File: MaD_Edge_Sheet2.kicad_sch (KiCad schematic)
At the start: 105 parts

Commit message: new Mad Edge being manufactured
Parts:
- removed C? (x6): 0.1uF, symbol Device:C_Small
- removed D? (x6): LED, symbol Device:LED
- removed IC, IC? (x3): NSI50010YT1G, symbol NSI50010YT1G:NSI50010YT1G
- removed IC?: ISO6742DWR, symbol ISO6742DWR:ISO6742DWR
- removed IC?: ISO6721BDR, symbol ISO6721BDR:ISO6721BDR
- removed J?: DYNPWR, symbol Connector_Generic:Conn_01x03
- removed J?: ServoCtrl, symbol Connector_Generic:Conn_01x10
- removed J?: Encoder, symbol Connector_Generic:Conn_01x10
- removed J?: ServoSerial, symbol Connector_Generic:Conn_01x05
- removed JP?: Z_GND, symbol Jumper:Jumper_2_Open
- removed JP?: ZI_GND, symbol Jumper:Jumper_2_Open
- removed JP?: A_GND, symbol Jumper:Jumper_2_Open
- removed JP?: TTL-SINK, symbol Jumper:Jumper_3_Open
- removed JP?: B_GND, symbol Jumper:Jumper_2_Open
- removed Q?: 2N3904, Package_TO_SOT_THT:TO-92_Inline, symbol Transistor_BJT:2N3904
- removed R? (x5): 1K, symbol Device:R_Small
- removed R? (x6): 220R, symbol Device:R_Small
- removed R?: 43K, symbol Device:R_Small
- removed U? (x2): VO2631, Package_DIP:DIP-8_W7.62mm, symbol Isolator:VO2631
- removed U?: AM26LS31CD, Package_SO:SOIC-16_3.9x9.9mm_P1.27mm, symbol Interface:AM26LS31CD
- added C13, C18, C19, C23, C7, C9: 0.1uF, Capacitor_SMD:C_0603_1608Metric, symbol Device:C_Small
- added C17, C5: 10uF, Capacitor_SMD:C_1206_3216Metric, symbol Device:C_Small
- added D10, D11, D13, D16, D5, D7, D8: LED, LED_SMD:LED_0603_1608Metric, symbol Device:LED
- added IC1: ISO6742DWR, ISO6742DWR:SOIC127P1030X265-16N, symbol ISO6742DWR:ISO6742DWR
- added IC12, IC13: NSI50010YT1G, NSI50010YT1G:SOD3716X135N, symbol NSI50010YT1G:NSI50010YT1G
- added IC3: UCC12040DVER, UCC12040DVER:SOIC127P1030X265-16N, symbol UCC12040DVER:UCC12040DVER
- added J10: ChargePump, Connector_Molex:Molex_Micro-Fit_3.0_43650-0321_1x03_P3.00mm_Vertical, symbol Connector_Generic:Conn_01x03
- added J17: GPI_3, Connector_Molex:Molex_Micro-Fit_3.0_43650-0321_1x03_P3.00mm_Vertical, symbol Connector_Generic:Conn_01x03
- added J18: GPI_4, Connector_Molex:Molex_Micro-Fit_3.0_43650-0321_1x03_P3.00mm_Vertical, symbol Connector_Generic:Conn_01x03
- added J5: GPO_2, Connector_Molex:Molex_Micro-Fit_3.0_43045-0415_2x02_P3.00mm_Vertical, symbol Connector_Generic:Conn_01x04
- added J6: GPO_1, Connector_Molex:Molex_Micro-Fit_3.0_43045-0415_2x02_P3.00mm_Vertical, symbol Connector_Generic:Conn_01x04
- added J7: GPI_2, Connector_Molex:Molex_Micro-Fit_3.0_43045-0415_2x02_P3.00mm_Vertical, symbol Connector_Generic:Conn_01x04
- added J8: GPI_1, Connector_Molex:Molex_Micro-Fit_3.0_43045-0415_2x02_P3.00mm_Vertical, symbol Connector_Generic:Conn_01x04
- added R11, R13, R14, R16, R17, R19, R22: 220R, Resistor_SMD:R_0603_1608Metric, symbol Device:R_Small
- added R38: 390R, Resistor_SMD:R_0603_1608Metric, symbol Device:R_Small
- added R4, R8: 1K, Resistor_SMD:R_0603_1608Metric, symbol Device:R_Small
- added U17: SN74LVC1G14DBV, Package_TO_SOT_SMD:SOT-23-5, symbol 74xGxx:SN74LVC1G14DBV
- added U4: 6N137, Package_DIP:DIP-8_W7.62mm, symbol Isolator:6N137
- added U8: VO2631, Package_DIP:DIP-8_W7.62mm, symbol Isolator:VO2631
- C10, C11, C12, C14, C15, C20, C21, C22, C8: renamed from C?; footprint (none) -> Capacitor_SMD:C_0603_1608Metric; DIGIKEY (none) -> 1276-1043-1-ND; LCSC (none) -> C14663; MANUFACTURER (none) -> Samsung Electro-Mechanics; Manufacturer_Part_Number (none) -> CL05A104KA5NNNC; manufacturer_1 (none) -> YAGEO; manufacturer_part_number_1 (none) -> CC0603KRX7R9BB104
- C16, C6: renamed from C?; footprint (none) -> Capacitor_SMD:C_1206_3216Metric; DIGIKEY (none) -> 1276-1181-1-ND; LCSC (none) -> C9807; MANUFACTURER (none) -> Samsung Electro-Mechanics; Manufacturer_Part_Number (none) -> CL31A106MAHNNNE; manufacturer_1 (none) -> Samsung Electro-Mechanics; manufacturer_part_number_1 (none) -> CL31A106KAHNNNE
- D12, D15, D3, D4, D6, D9: renamed from D?; footprint (none) -> LED_SMD:LED_0603_1608Metric; DIGIKEY (none) -> 160-1435-1-ND; LCSC (none) -> C193901; MANUFACTURER (none) -> Lite-On Inc.; Manufacturer_Part_Number (none) -> LTST-C190KGKT; manufacturer_1 (none) -> Foshan NationStar Optoelectronics; manufacturer_part_number_1 (none) -> NCD0603C2
- IC10, IC11, IC6, IC7, IC8, IC9: renamed from IC?; footprint (none) -> NSI50010YT1G:SOD3716X135N; DIGIKEY (none) -> NSI50010YT1G; Datasheet_1 http://www.onsemi.com/pub/Collateral/NSI50010Y-D.PDF -> (none); Footprint_1 SOD3716X135N -> (none); LCSC (none) -> C150049; MANUFACTURER (none) -> onsemi; Manufacturer_Name onsemi -> (none); Mouser Part Number 863-NSI50010YT1G -> (none); Mouser Price/Stock https://www.mouser.co.uk/ProductDetail/onsemi/NSI50010YT1G?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 -> (none); Reference_1 D -> (none); Value_1 NSI50010YT1G -> (none); manufacturer_1 (none) -> onsemi; manufacturer_part_number_1 (none) -> NSI50010YT1G
- IC2: renamed from IC?; footprint (none) -> ISO6742DWR:SOIC127P1030X265-16N; DIGIKEY (none) -> 296-ISO6742DWRCT-ND; Datasheet_1 https://www.ti.com/lit/ds/symlink/iso6742.pdf?ts=1647643759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 -> (none); Footprint_1 SOIC127P1030X265-16N -> (none); LCSC (none) -> C2862403; MANUFACTURER (none) -> Texas Instruments; Manufacturer_Name Texas Instruments -> (none); Mouser Part Number 595-ISO6742DWR -> (none); Mouser Price/Stock https://www.mouser.co.uk/ProductDetail/Texas-Instruments/IS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 -> (none); NOTES (none) -> Pin Compatible with ISO77xx; Reference_1 IC -> (none); Value_1 ISO6742DWR -> (none); manufacturer_1 (none) -> Texas Instruments; manufacturer_part_number_1 (none) -> ISO6742DWR or ISO7742FDWR
- IC4: renamed from IC?; footprint (none) -> UCC12040DVER:SOIC127P1030X265-16N; DIGIKEY (none) -> 296-UCC12040DVERCT-ND; Datasheet_1 https://www.ti.com/lit/gpn/ucc12040?HQS=ti-null-null-sf-df-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 -> (none); Footprint_1 SOIC127P1030X265-16N -> (none); LCSC (none) -> C507279; MANUFACTURER (none) -> Texas Instruments; Manufacturer_Name Texas Instruments -> (none); Mouser Part Number 595-UCC12040DVER -> (none); Mouser Price/Stock https://www.mouser.co.uk/ProductDetail/Texas-Instruments/UC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 -> (none); Reference_1 IC -> (none); Value_1 UCC12040DVER -> (none); manufacturer_1 (none) -> Texas Instruments; manufacturer_part_number_1 (none) -> UCC12040DVE
- IC5: renamed from IC?; footprint (none) -> ISO6731DWR:SOIC127P1030X265-16N; DIGIKEY (none) -> 296-ISO6731DWRCT-ND; Datasheet_1 https://www.ti.com/lit/ds/symlink/iso6731.pdf?ts=1623477624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 -> (none); Footprint_1 SOIC127P1030X265-16N -> (none); LCSC (none) -> C2861559; MANUFACTURER (none) -> Texas Instruments; Manufacturer_Name Texas Instruments -> (none); Mouser Part Number 595-ISO6731DWR -> (none); Mouser Price/Stock https://www.mouser.co.uk/ProductDetail/Texas-Instruments/IS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 -> (none); NOTES (none) -> Pin Compatible with ISO77xx; Reference_1 IC -> (none); Value_1 ISO6731DWR -> (none); manufacturer_1 (none) -> Texas Instruments; manufacturer_part_number_1 (none) -> ISO6731DWR or ISO7731DW
- J11, J12, J13, J14, J16: renamed from J?; footprint (none) -> Connector_Molex:Molex_Micro-Fit_3.0_43650-0321_1x03_P3.00mm_Vertical; DIGIKEY (none) -> WM14311CT-ND; LCSC (none) -> C277374; MANUFACTURER (none) -> Molex; Manufacturer_Part_Number (none) -> 0436500321; manufacturer_1 (none) -> MOLEX; manufacturer_part_number_1 (none) -> 436500321
- J15: renamed from J?; value ESDLower -> ENDLower; footprint (none) -> Connector_Molex:Molex_Micro-Fit_3.0_43650-0321_1x03_P3.00mm_Vertical; DIGIKEY (none) -> WM14311CT-ND; LCSC (none) -> C277374; MANUFACTURER (none) -> Molex; Manufacturer_Part_Number (none) -> 0436500321; manufacturer_1 (none) -> MOLEX; manufacturer_part_number_1 (none) -> 436500321
- J19: renamed from J?; footprint (none) -> Connector_Molex:Molex_Micro-Fit_3.0_43650-0521_1x05_P3.00mm_Vertical; DIGIKEY (none) -> WM14316CT-ND; LCSC (none) -> C277377; MANUFACTURER (none) -> Molex; Manufacturer_Part_Number (none) -> 0436500521; manufacturer_1 (none) -> MOLEX; manufacturer_part_number_1 (none) -> 436500521
- J4: renamed from J?; footprint (none) -> Connector_Molex:Molex_Micro-Fit_3.0_43045-0618_2x03-1MP_P3.00mm_Vertical; DIGIKEY (none) -> WM1803CT-ND; LCSC (none) -> C240837; MANUFACTURER (none) -> Molex; Manufacturer_Part_Number (none) -> 0430450618; manufacturer_1 (none) -> MOLEX; manufacturer_part_number_1 (none) -> 430450618
- J9: renamed from J?; footprint (none) -> Connector_Molex:Molex_Micro-Fit_3.0_43045-0615_2x03_P3.00mm_Vertical; DIGIKEY (none) -> WM6688CT-ND; LCSC (none) -> C563823; MANUFACTURER (none) -> Molex; Manufacturer_Part_Number (none) -> 0430450615; manufacturer_1 (none) -> MOLEX; manufacturer_part_number_1 (none) -> 430450615
- R1, R2, R3, R5, R6, R7: renamed from R?; footprint (none) -> Resistor_SMD:R_0603_1608Metric; LCSC (none) -> C21190; manufacturer_1 (none) -> UNI-ROYAL(Uniroyal Elec); manufacturer_part_number_1 (none) -> 0603WAF1001T5E
- R10, R12, R15, R18, R21, R9: renamed from R?; footprint (none) -> Resistor_SMD:R_0603_1608Metric; LCSC (none) -> C22962; manufacturer_1 (none) -> UNI-ROYAL(Uniroyal Elec); manufacturer_part_number_1 (none) -> 0603WAF2200T5E
- U10, U11, U12, U13, U14, U15, U16, U18, U19, U21, U22, U9: renamed from U?; LCSC (none) -> C5250998; MANUFACTURER (none) -> Texas Instruments; Manufacturer_Part_Number (none) -> SN74LVC1G14DBVT; manufacturer_1 (none) -> TWGMC; manufacturer_part_number_1 (none) -> SN74LVC1G14DBVR
- U5, U6, U7: renamed from U?; MANUFACTURER (none) -> Vishay Semiconductor Opto Division; Manufacturer_Part_Number (none) -> VO2631; manufacturer_1 (none) -> Vishay Intertech; manufacturer_part_number_1 (none) -> VO2631
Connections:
- net VIO_00_07 is gone; now on net +3.3V: C11.1, IC5.16 (VCC2)
- net VIO_48_55 is gone; now on net +3.3V: C10.1, IC2.1 (VCC1)
- net +3.3V: now also C9.1, IC1.1 (VCC1), R13.1, R16.1, R17.1, R19.1, R22.1, U17.5 (VCC)
- net +5V: now also C23.2, C5.1, C7.1, IC3.1 (EN), IC3.3 (VINP), U8.8 (VCC)
- net GND: now also C23.1, C5.2, C7.2, C9.2, D5.1 (K), D8.1 (K), IC1.2 (GND1_1), IC1.8 (GND1_2), IC3.2 (GNDP), IC3.4 (SYNC), IC3.6 (NC_1), IC3.7 (NC_2), IC3.8 (NC_3), U17.3 (GND), U4.3 (C), U8.5 (GND)
- net IDOOR+: now also IC9.2 (A); no longer IC11.2 (A)
- net IDOOR-: now also U6.3 (C2); no longer U7.3 (C2)
- net IEND_L+: now also J15.2 (Pin_2); no longer J15.1 (Pin_1)
- net IEND_L-: now also J15.1 (Pin_1); no longer J15.2 (Pin_2)
- net IEND_U+: now also IC11.2 (A); no longer IC9.2 (A)
- net IEND_U-: now also U7.3 (C2); no longer U6.3 (C2)
- net IESD_A+: now also J13.2 (Pin_2); no longer J13.1 (Pin_1)
- net IESD_A-: now also J13.1 (Pin_1); no longer J13.2 (Pin_2)
- net IESD_U+: now also J11.2 (Pin_2); no longer IC7.2 (A), J11.1 (Pin_1), J12.2 (Pin_2)
- net IESD_U-: now also J11.1 (Pin_1); no longer J11.2 (Pin_2)
- net P0: now also IC5.14 (OUTA); no longer IC5.12 (INC)
- net P1: now also IC5.13 (OUTB), U17.2; no longer IC5.14 (OUTA)
- net P13: now also J19.4 (Pin_4); no longer J19.2 (Pin_2)
- net P15: now also J19.2 (Pin_2); no longer J19.4 (Pin_4)
- net P16: no longer R6.2, R7.2, U15.2, U21.2, U6.7 (VO1), U7.7 (VO1)
- net P17: no longer R2.2, R3.2, U10.2, U18.2, U6.6 (VO2), U7.6 (VO2)
- net P2: now also IC5.12 (INC); no longer IC5.13 (OUTB)
- net P53: now also IC2.5 (OUTC); no longer IC2.4 (INB)
- net P54: now also IC2.4 (INB); no longer IC2.5 (OUTC)
- net RPI_GND: now also C12.2, IC2.15 (GND2_2), IC2.9 (GND2_1)
- net SHIELD: now also J10.3 (Pin_3), J17.3 (Pin_3), J18.3 (Pin_3), J5.4 (Pin_4), J6.4 (Pin_4), J7.4 (Pin_4), J8.4 (Pin_4)
- net VIO_16_23: now also R4.1, R8.1
- net at U19.4: now also D13.1 (K)
- net P23: now reaches U14.2
- net P23: now also R4.2, U8.6 (VO2)
- net at U14.4: now also R14.1
- net at U16.4: now also D10.1 (K)
- net P22: now reaches U11.2
- net P22: now also R8.2, U8.7 (VO1)
- net at U11.4: now also R11.1
- net at U22.4: now also D16.1 (K)
- net at U13.4: now also D7.1 (K)
- net FG_5V renamed IFG_5V
- net FG_GND renamed IFG_GND
- net FG_INT renamed IFG_INT
- net FG_RX renamed IFG_RX
- net FG_TX renamed IFG_TX
- net P10 renamed P27
- net P27: now also IC1.3 (INA)
- net P11 renamed P24
- net P24: now also IC1.6 (OUTD)
- net P12 renamed P25
- net P25: now also IC1.5 (OUTC)
- net P9 renamed P26
- net P26: now also IC1.4 (INB)
- new net: D13.2 (A), R19.2
- new net: D7.2 (A), R13.2
- new net: D8.2 (A), R14.2
- new net: IC12.1 (K), U8.1 (A1)
- new net: IC13.1 (K), U8.4 (A2)
- new net: D5.2 (A), R11.2
- new net: D11.2 (A), R17.2
- new net: D11.1 (K), U17.4
- new net: D16.2 (A), R22.2
- new net: D10.2 (A), R16.2
- new net: J10.1 (Pin_1), U4.6 (VO)
- new net: R38.2, U4.2 (A)
- new net 5V_IO: C13.1, C17.2, C18.2, C19.1, IC1.16 (VCC2), IC3.13 (SEL), IC3.14 (VISO), J5.1 (Pin_1), J6.1 (Pin_1), J7.1 (Pin_1), J8.1 (Pin_1), U4.7 (EN), U4.8 (VCC)
- new net GND_IO: C13.2, C17.1, C18.1, C19.2, IC1.15 (GND2_2), IC1.9 (GND2_1), IC3.10 (NC_4), IC3.11 (NC_5), IC3.12 (NC_6), IC3.15 (GNDS_2), IC3.16 (GNDS_3), IC3.9 (GNDS_1), J10.2 (Pin_2), J5.3 (Pin_3), J6.3 (Pin_3), J7.3 (Pin_3), J8.3 (Pin_3), U4.5 (GND)
- new net GPI_3+: IC12.2 (A), J17.2 (Pin_2)
- new net GPI_3-: J17.1 (Pin_1), U8.2 (C1)
- new net GPI_4+: IC13.2 (A), J18.2 (Pin_2)
- new net GPI_4-: J18.1 (Pin_1), U8.3 (C2)
- new net IESD_L+: IC7.2 (A), J12.2 (Pin_2)
- new net IGPI1: IC1.11 (IND), J8.2 (Pin_2)
- new net IGPI2: IC1.12 (INC), J7.2 (Pin_2)
- new net IGPO1: IC1.13 (OUTB), J6.2 (Pin_2)
- new net IGPO2: IC1.14 (OUTA), J5.2 (Pin_2)
- new net P18: R6.2, U15.2, U6.7 (VO1)
- new net P19: R2.2, U18.2, U6.6 (VO2)
- new net P20: R7.2, U21.2, U7.7 (VO1)
- new net P21: R3.2, U10.2, U7.6 (VO2)
- new net P28: R38.1
- no-connect marks 15 -> 10
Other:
- note removed: "How do deal with shielding?"
- note removed: "Need to use same GPI setup for ESD and regular endstops/door"
- moved on the sheet: C20, C21, C22, D12, D15, D3, D4, D6, D9, IC10, IC11, IC6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

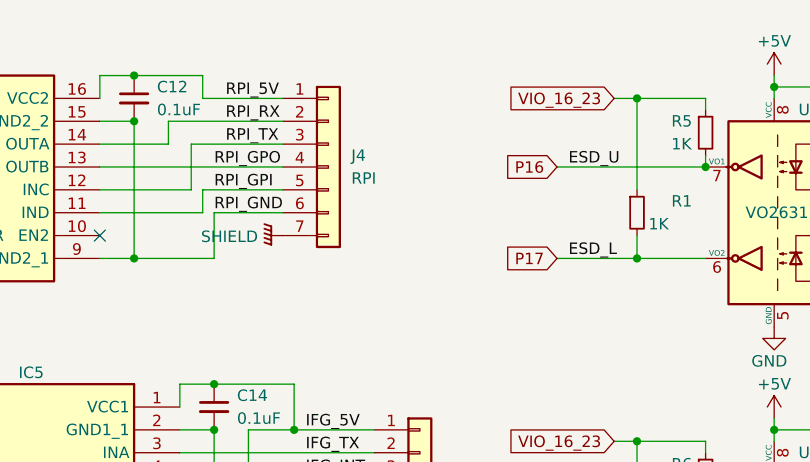
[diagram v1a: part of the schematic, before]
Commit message: working version for getting basic data for the thesis
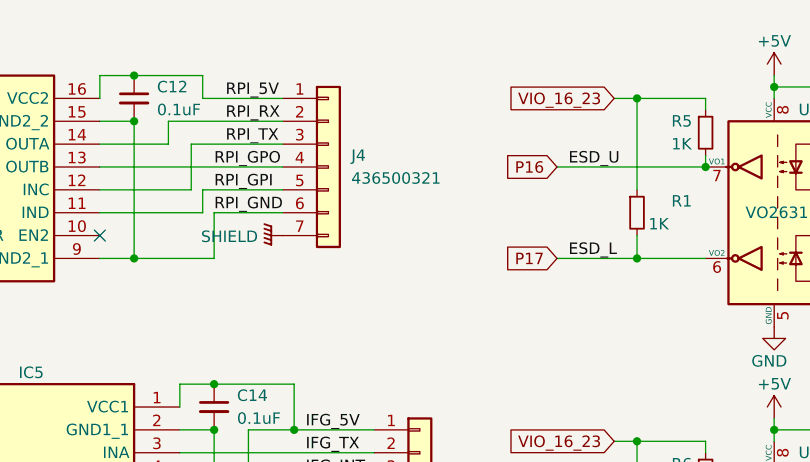
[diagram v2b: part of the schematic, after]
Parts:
- C10, C11, C12, C13, C14, C15, C18, C19, C20, C21, C22, C23, C7, C8, C9, R1, R2, R3, R38, R4, R5, R6, R7, R8: Qty Bought (none) -> 100 - lcsc
- C16, C17, C5, C6: Qty Bought (none) -> 20 - lcsc
- D10, D11, D12, D13, D15, D16, D3, D4, D5, D6, D7, D8, D9: Qty Bought (none) -> 80 - lcsc
- IC1, IC2: Qty Bought (none) -> 10 digikey
- IC10, IC11, IC12, IC13, IC6, IC7, IC8, IC9: Qty Bought (none) -> 35 - lcsc
- IC3, IC4: Qty Bought (none) -> 3 digikey
- IC5: Qty Bought (none) -> 3 - lcsc
- J10: Qty Bought (none) -> 2 - lcsc (buy digikey also); Receptical (none) -> 0436450300
- J19: Qty Bought (none) -> 6 - lcsc; Receptical (none) -> 0436450500
- J4: value RPI -> 436500321; Qty Bought (none) -> 4 - lcsc; Receptical (none) -> 0430250600
- J5: Qty Bought (none) -> 10 - digikey; Receptical (none) -> 0430250400
- J9: Qty Bought (none) -> 4 - lcsc; Receptical (none) -> 0430250600
- R10, R11, R12, R13, R14, R15, R16, R17, R18, R19, R21, R22, R9: Qty Bought (none) -> 200 - lcsc
- U10, U11, U12, U13, U14, U15, U16, U17, U18, U19, U21, U22, U9: Qty Bought (none) -> 100 lcsc
- U4: Qty Bought (none) -> 4 - lcsc
- U5, U6, U7, U8: LCSC (none) -> C511606; Qty Bought (none) -> 12 - lcsc
